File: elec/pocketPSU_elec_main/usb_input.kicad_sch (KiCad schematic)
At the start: 0 parts

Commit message: add esp32 micro
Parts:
- added R12, R13: 5.1K, symbol Device:R_Small
- added USB1: KH-TYPE-C-16P, footprints:USB-C-SMD_KH-TYPE-C-16P, symbol footprints:KH-TYPE-C-16P
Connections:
- new net: R13.1, USB1.B5 (CC2)
- new net: R12.1, USB1.A5 (CC1)
- new net GND: R12.2, R13.2, USB1.1 (EP), USB1.2 (EP), USB1.3 (EP), USB1.4 (EP), USB1.A1 (GND), USB1.A12 (GND), USB1.B1 (GND), USB1.B12 (GND)
- new net USB_DM: USB1.A7 (DN1), USB1.B7 (DN2)
- new net USB_DP: USB1.A6 (DP1), USB1.B6 (DP2)
- new net VBUS: USB1.A4 (VBUS), USB1.A9 (VBUS), USB1.B4 (VBUS), USB1.B9 (VBUS)

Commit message: preliminary layout
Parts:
- R12, R13: footprint (none) -> Resistor_SMD:R_0402_1005Metric
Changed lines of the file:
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@@
 			)
 		)
-		(property "Footprint" ""
+		(property "Footprint" "Resistor_SMD:R_0402_1005Metric"
 			(at 191.77 96.52 0)
 			(effects
@@
 			)
 		)
-		(property "Footprint" ""
+		(property "Footprint" "Resistor_SMD:R_0402_1005Metric"
 			(at 101.6 91.44 0)
 			(effects

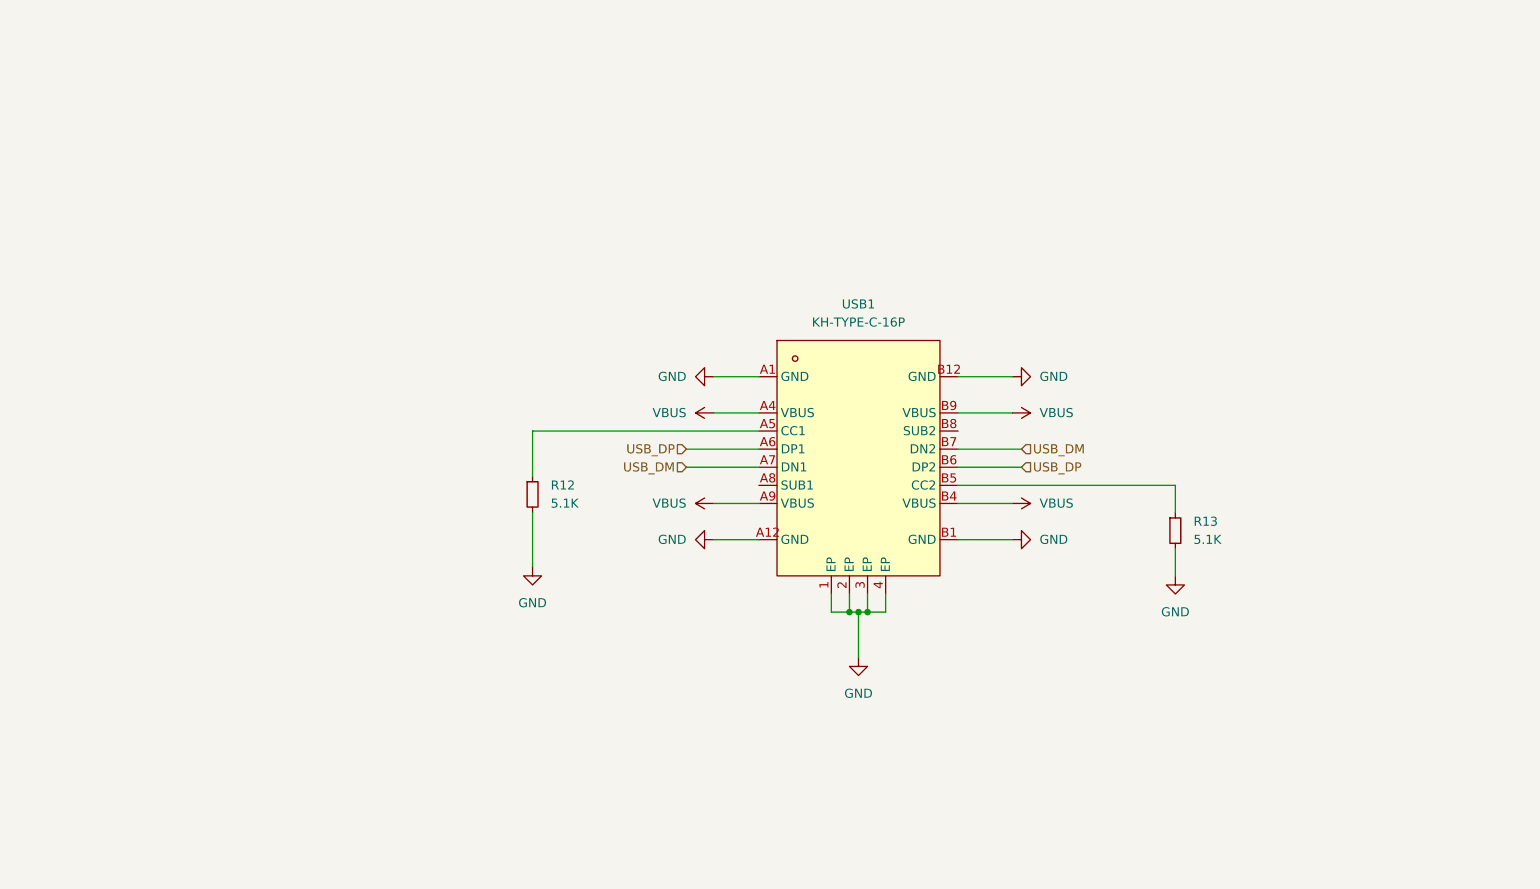
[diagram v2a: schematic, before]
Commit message: add usb coms chip
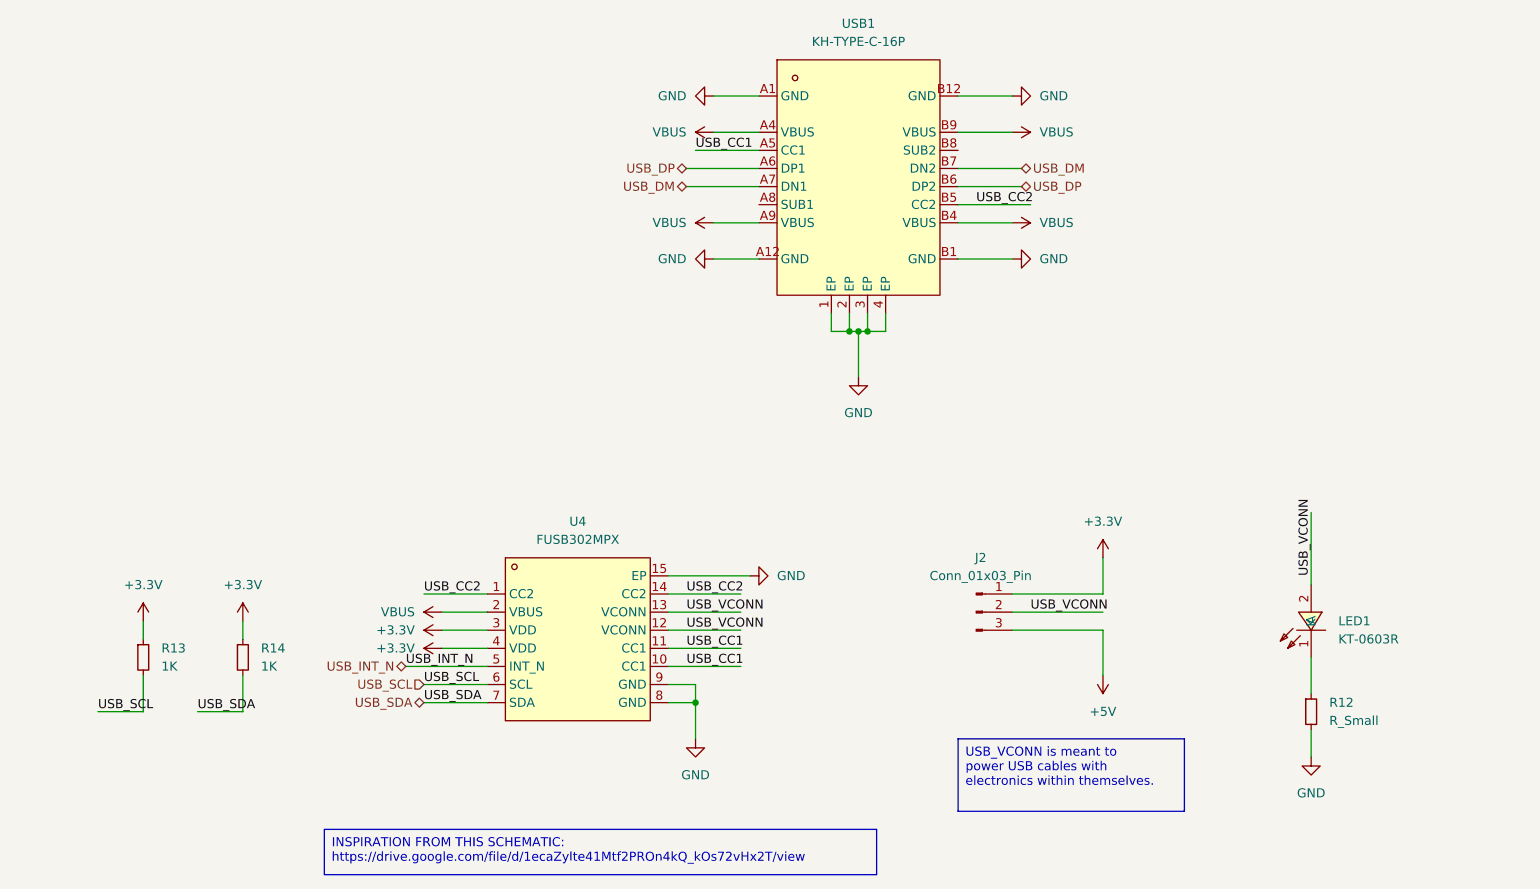
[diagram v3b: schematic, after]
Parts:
- added J2: Conn_01x03_Pin, symbol Connector:Conn_01x03_Pin
- added LED1: KT-0603R, footprints:LED0603-RD, symbol footprints:KT-0603R
- added R14: 1K, symbol Device:R_Small
- added U4: FUSB302MPX, footprints:MLP-14_L2.5-W2.5-P0.50-BL-EP, symbol footprints:FUSB302MPX
- R12: value 5.1K -> R_Small; footprint Resistor_SMD:R_0402_1005Metric -> (none)
- R13: value 5.1K -> 1K; footprint Resistor_SMD:R_0402_1005Metric -> (none)
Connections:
- net GND: now also U4.15 (EP), U4.8 (GND), U4.9 (GND); no longer R13.2
- net VBUS: now also U4.2 (VBUS)
- net +3.3V: now reaches R13.1
- net +3.3V: now also J2.1 (Pin_1), R14.1, U4.3 (VDD), U4.4 (VDD); no longer USB1.B5 (CC2)
- net at R12.1: now also LED1.1 (K); no longer USB1.A5 (CC1)
- new net +5V: J2.3 (Pin_3)
- new net USB_CC1: U4.10 (CC1), U4.11 (CC1), USB1.A5 (CC1)
- new net USB_CC2: U4.1 (CC2), U4.14 (CC2), USB1.B5 (CC2)
- new net USB_INT_N: U4.5 (INT_N)
- new net USB_SCL: R13.2, U4.6 (SCL)
- new net USB_SDA: R14.2, U4.7 (SDA)
- new net USB_VCONN: J2.2 (Pin_2), LED1.2 (A), U4.12 (VCONN), U4.13 (VCONN)
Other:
- moved on the sheet: USB1

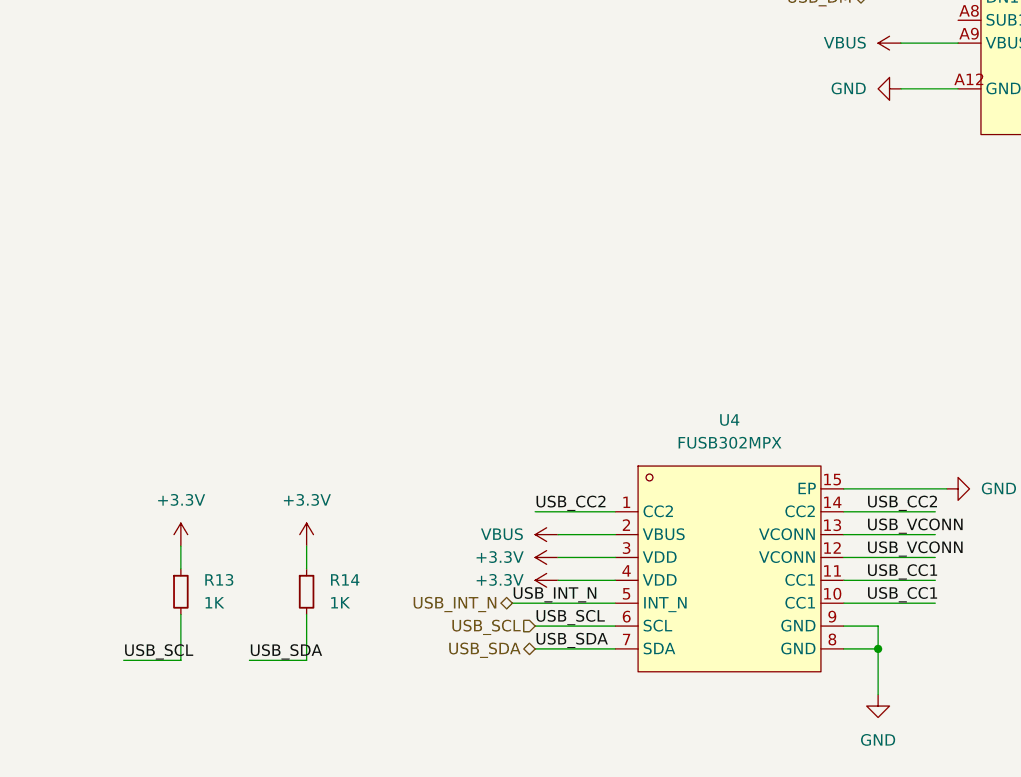
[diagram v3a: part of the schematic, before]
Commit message: add bypass caps on usb coms chip
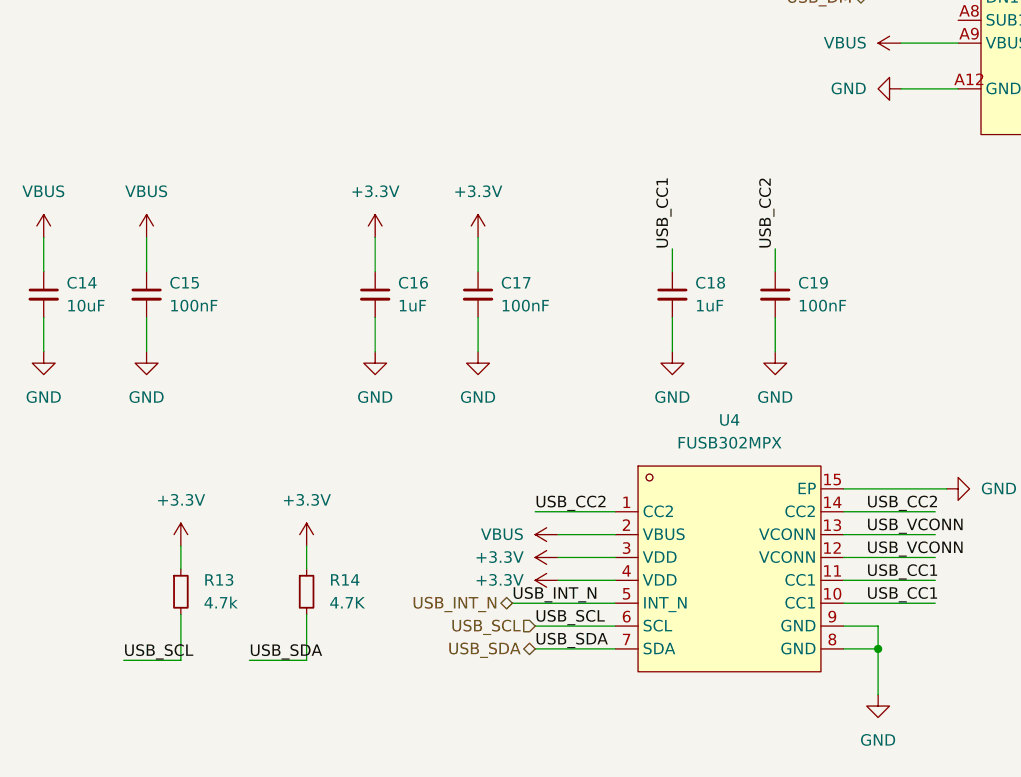
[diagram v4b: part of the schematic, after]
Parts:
- added C14: 10uF, Capacitor_SMD:C_0805_2012Metric, symbol Device:C_Small
- added C15, C17, C19: 100nF, Capacitor_SMD:C_0805_2012Metric, symbol Device:C_Small
- added C16, C18: 1uF, Capacitor_SMD:C_0805_2012Metric, symbol Device:C_Small
- R13: value 1K -> 4.7k
- R14: value 1K -> 4.7K
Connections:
- net +3.3V: now also C16.1, C17.1
- net GND: now also C14.2, C15.2, C16.2, C17.2, C18.2, C19.2
- net USB_CC1: now also C18.1
- net USB_CC2: now also C19.1
- net VBUS: now also C14.1, C15.1

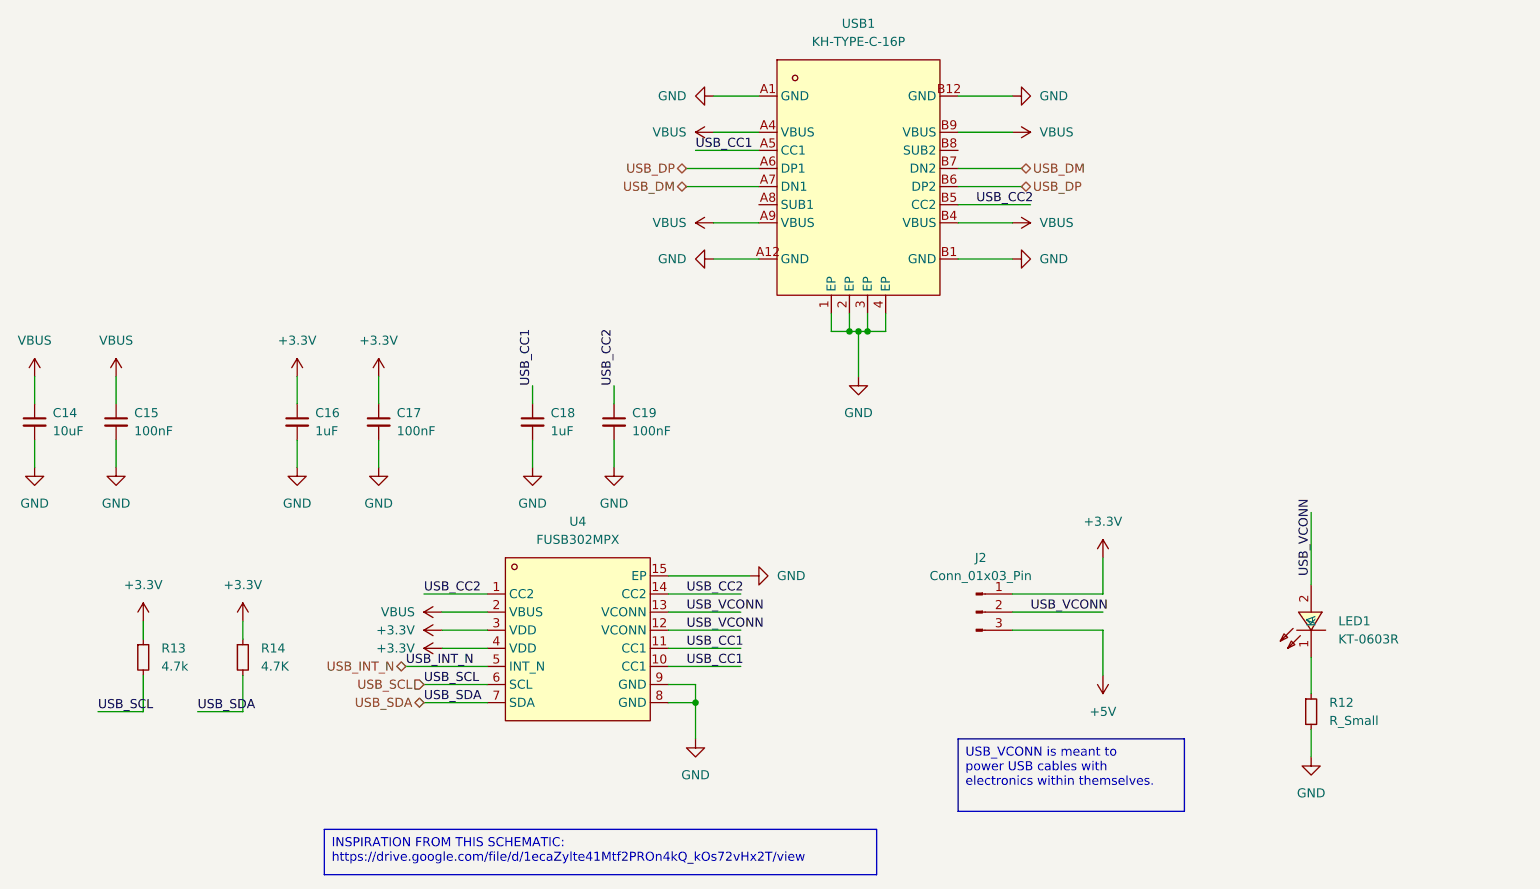
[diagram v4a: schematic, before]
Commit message: fix caps values, rework layout
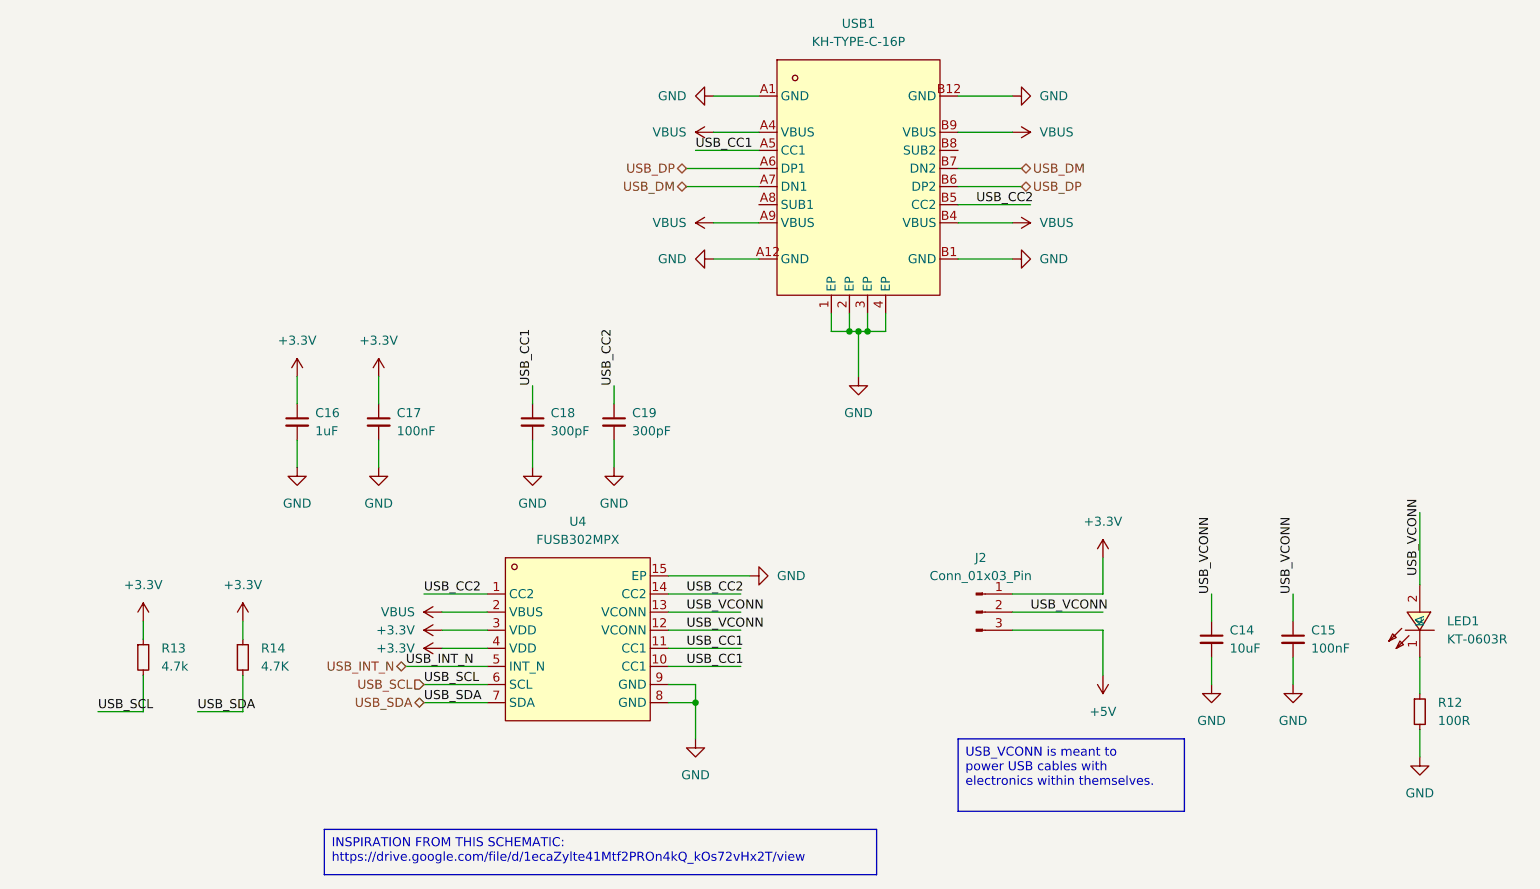
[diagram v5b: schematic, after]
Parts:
- C18: value 1uF -> 300pF
- C19: value 100nF -> 300pF
- J2: footprint (none) -> Connector_PinHeader_1.27mm:PinHeader_1x03_P1.27mm_Vertical
- R12: value R_Small -> 100R; footprint (none) -> Resistor_SMD:R_0402_1005Metric
- R13, R14: footprint (none) -> Resistor_SMD:R_0402_1005Metric
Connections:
- net USB_VCONN: now also C14.1, C15.1
- net VBUS: no longer C14.1, C15.1
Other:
- moved on the sheet: C14, C15, LED1, R12

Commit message: add copper fill
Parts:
- added TPCC1, TPCC2: TestPoint, TestPoint:TestPoint_Pad_D1.5mm, symbol Connector:TestPoint
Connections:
- net USB_CC1: now also TPCC1.1
- net USB_CC2: now also TPCC2.1
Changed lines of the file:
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@@
-	(wire
-		(pts
-			(xy 124.46 43.18) (xy 133.35 43.18)
-		)
-		(stroke
-			(width 0)
-			(type default)
-		)
-	)
 	(wire
 		(pts
@@
 	(wire
 		(pts
+			(xy 114.3 43.18) (xy 133.35 43.18)
+		)
+		(stroke
+			(width 0)
+			(type default)
+		)
+	)
+	(wire
+		(pts
 			(xy 68.58 74.93) (xy 68.58 78.74)
 		)
@@
 	(wire
 		(pts
-			(xy 161.29 50.8) (xy 171.45 50.8)
+			(xy 161.29 50.8) (xy 180.34 50.8)
 		)
 		(stroke
@@
 	)
 	(symbol
+		(lib_id "Connector:TestPoint")
+		(at 180.34 50.8 270)
+		(unit 1)
+		(exclude_from_sim no)
+		(in_bom yes)
+		(on_board yes)
+		(dnp no)
+		(fields_autoplaced yes)
+		(property "Reference" "TPCC2"
+			(at 185.42 49.5299 90)
+			(effects
+				(font
+					(size 1.27 1.27)
+				)
+				(justify left)
+			)
+		)
+		(property "Value" "TestPoint"
+			(at 185.42 52.0699 90)
+			(effects
+				(font
+					(size 1.27 1.27)
+				)
+				(justify left)
+			)
+		)
+		(property "Footprint" "TestPoint:TestPoint_Pad_D1.5mm"
+			(at 180.34 55.88 0)
+			(effects
+				(font
+					(size 1.27 1.27)
+				)
+				(hide yes)
+			)
+		)
+		(property "Datasheet" "~"
+			(at 180.34 55.88 0)
+			(effects
+				(font
+					(size 1.27 1.27)
+				)
+				(hide yes)
+			)
+		)
+		(property "Description" "test point"
+			(at 180.34 50.8 0)
+			(effects
+				(font
+					(size 1.27 1.27)
+				)
+				(hide yes)
+			)
+		)
+		(pin "1"
+		)
+		(instances
+			(project "pocketPSU_elec_main"
+				(path "/439011d5-4dd5-4d65-a9bd-b0be402d54a5/6a8f7395-3ccf-431e-bc54-d9f688783b5c"
+					(reference "TPCC2")
+					(unit 1)
+				)
+			)
+		)
+	)
+	(symbol
 		(lib_id "Device:C_Small")
 		(at 113.03 81.28 0)
@@
 					(unit 1)
 				)
+			)
+		)
+	)
+	(symbol
+		(lib_id "Connector:TestPoint")
+		(at 114.3 43.18 90)
+		(unit 1)
+		(exclude_from_sim no)
+		(in_bom yes)
+		(on_board yes)
+		(dnp no)
+		(fields_autoplaced yes)
+		(property "Reference" "TPCC1"
+			(at 110.998 38.1 90)
+			(effects
+				(font
+					(size 1.27 1.27)
+				)
+			)
+		)
+		(property "Value" "TestPoint"
+			(at 110.998 40.64 90)
+			(effects
+				(font
+					(size 1.27 1.27)
+				)
+			)
+		)
+		(property "Footprint" "TestPoint:TestPoint_Pad_D1.5mm"
+			(at 114.3 38.1 0)
+			(effects
+				(font
+					(size 1.27 1.27)
+				)
+				(hide yes)
+			)
+		)
+		(property "Datasheet" "~"
+			(at 114.3 38.1 0)
+			(effects
+				(font
+					(size 1.27 1.27)
+				)
+				(hide yes)
+			)
+		)
+		(property "Description" "test point"
+			(at 114.3 43.18 0)
+			(effects
+				(font
+					(size 1.27 1.27)
+				)
+				(hide yes)
+			)
+		)
+		(pin "1"
+		)
+		(instances
+			(project "pocketPSU_elec_main"
+				(path "/439011d5-4dd5-4d65-a9bd-b0be402d54a5/6a8f7395-3ccf-431e-bc54-d9f688783b5c"
+					(reference "TPCC1")
+					(unit 1)
+				)
